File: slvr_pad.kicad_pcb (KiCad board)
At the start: 2 copper layers, 24 parts, among them SW1 SW_Push, U1 ATmega32U4-AU, Y1 16MHz

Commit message: PCB: Route all traces
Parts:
- moved C6 9.53 mm to (156.4, 93.7), turned to 90 degrees
- moved C7 9.53 mm to (146.8, 93.7), turned to 270 degrees
- moved C4 4.83 mm to (142.9, 96.0)
- moved USB1 3.18 mm to (146.8, 81.0)
- moved R4 2.86 mm to (138.1, 100.0), turned to 90 degrees
- moved R2 1.60 mm to (141.3, 90.5)
- moved C1 1.59 mm to (138.1, 104.0)
- moved R3 1.59 mm to (138.1, 90.5)
- turned D3 to 90 degrees
- turned D4 to 90 degrees
- turned Y1 to 180 degrees
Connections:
- D2 pad 1: ROW1 -> ROW0
- D3 pad 1: ROW0 -> ROW1
- MX2 pad 1: COL0 -> COL1
- MX3 pad 1: COL1 -> COL0
- U1 pad 27: Net-(U1-Pad27) -> ROW0
- U1 pad 28: Net-(U1-Pad28) -> COL0
- U1 pad 29: Net-(U1-Pad29) -> ROW1
- U1 pad 30: Net-(U1-Pad30) -> COL1
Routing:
- net GND: track 0.00 -> 121.2 mm, vias 0 -> 2
- net +5V: track 0.00 -> 119.9 mm, vias 0 -> 7
- net COL1: track 0.00 -> 52.1 mm, vias 0 -> 1
- net ROW0: track 0.00 -> 50.1 mm, vias 0 -> 3
- net ROW1: track 0.00 -> 46.9 mm, vias 0 -> 3
- net COL0: track 0.00 -> 30.2 mm, vias 0 -> 1
- net Net-(R4-Pad2): track 0.00 -> 23.3 mm, vias 0 -> 2
- net Net-(R2-Pad1): track 0.00 -> 22.2 mm
- net Net-(R3-Pad1): track 0.00 -> 22.0 mm
- net VCC: track 0.00 -> 13.1 mm
- net Net-(C6-Pad1): track 0.00 -> 12.0 mm
- net Net-(C7-Pad1): track 0.00 -> 11.8 mm
- net D-: track 0.00 -> 10.5 mm
- net D+: track 0.00 -> 7.99 mm
- net Net-(D4-Pad2): track 0.00 -> 6.62 mm
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
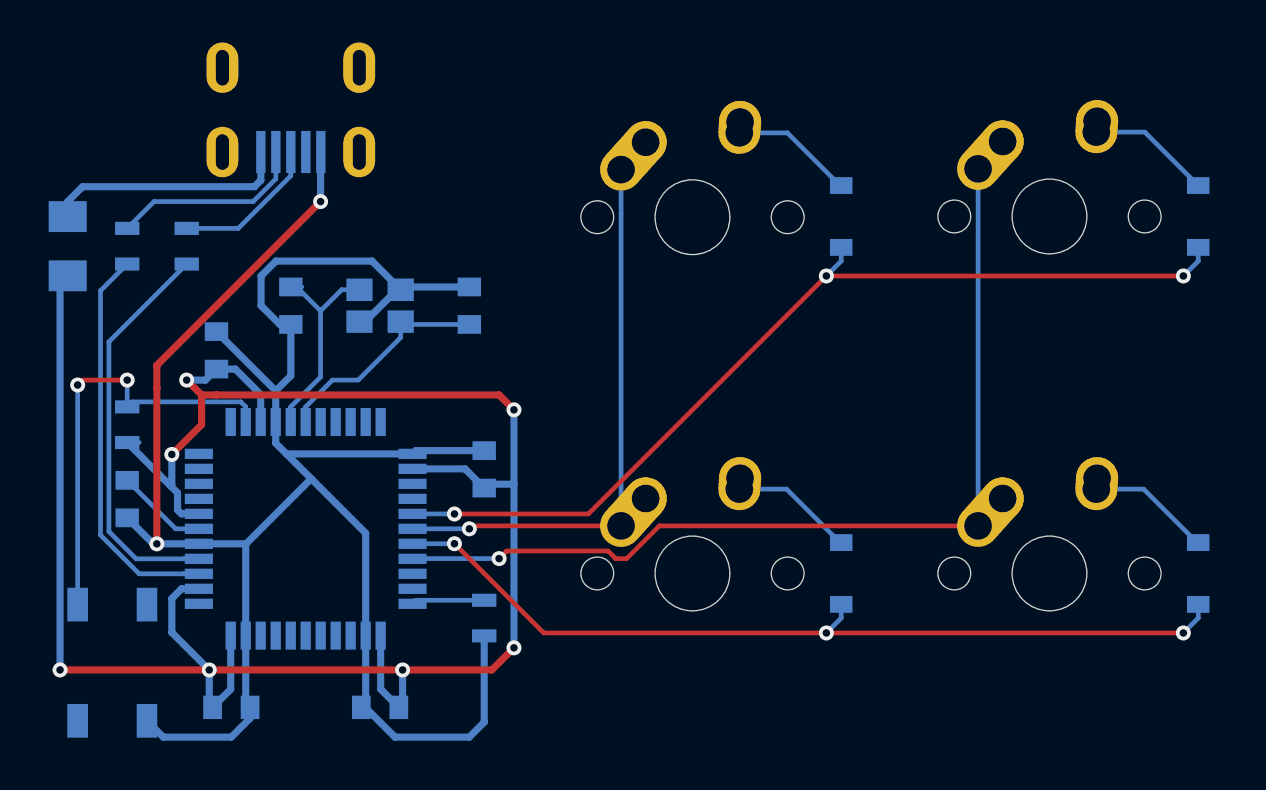
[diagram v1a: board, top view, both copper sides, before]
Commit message: PCB: Add ground fill
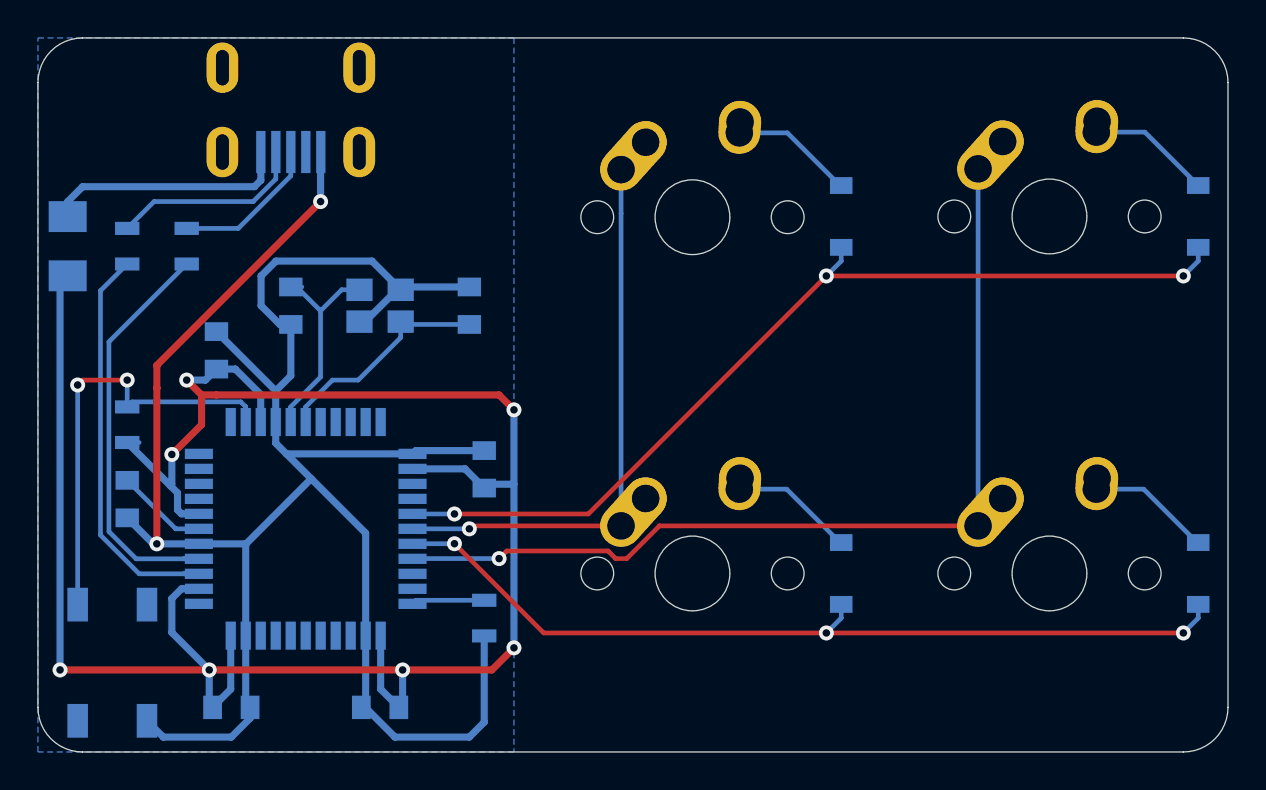
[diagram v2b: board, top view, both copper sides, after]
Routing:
- added copper zone on B.Cu, net GND
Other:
- board outline added: 63.5 x 38.1 mm
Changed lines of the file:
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@@
     (pad_to_mask_clearance 0.05)
     (aux_axis_origin 0 0)
-    (visible_elements FFFFFF7F)
+    (visible_elements FFFDFF7F)
     (pcbplotparams
       (layerselection 0x010fc_ffffffff)
@@
   )
   (module MX_Alps_Hybrid:MX-1U-NoLED (layer F.Cu)
+    (at 187.325 88.9)
+    (fp_text reference MX2 (at 0 3.175) (layer Dwgs.User)
+      (effects (font (size 1 1) (thickness 0.15)))
+    )
+    (fp_text value MX-NoLED (at 0 -7.9375) (layer Dwgs.User)
+      (effects (font (size 1 1) (thickness 0.15)))
+    )
+    (fp_line (start 5 -7) (end 7 -7) (layer Dwgs.User) (width 0.15))
+    (fp_line (start 7 -7) (end 7 -5) (layer Dwgs.User) (width 0.15))
+    (fp_line (start 5 7) (end 7 7) (layer Dwgs.User) (width 0.15))
+    (fp_line (start 7 7) (end 7 5) (layer Dwgs.User) (width 0.15))
+    (fp_line (start -7 5) (end -7 7) (layer Dwgs.User) (width 0.15))
+    (fp_line (start -7 7) (end -5 7) (layer Dwgs.User) (width 0.15))
+    (fp_line (start -5 -7) (end -7 -7) (layer Dwgs.User) (width 0.15))
+    (fp_line (start -7 -7) (end -7 -5) (layer Dwgs.User) (width 0.15))
+    (fp_line (start -9.525 -9.525) (end 9.525 -9.525) (layer Dwgs.User) (width 0.15))
+    (fp_line (start 9.525 -9.525) (end 9.525 9.525) (layer Dwgs.User) (width 0.15))
+    (fp_line (start 9.525 9.525) (end -9.525 9.525) (layer Dwgs.User) (width 0.15))
+    (fp_line (start -9.525 9.525) (end -9.525 -9.525) (layer Dwgs.User) (width 0.15))
+    (pad "" np_thru_hole circle (at 5.08 0 48.0996) (size 1.75 1.75) (drill 1.75) (layers *.Cu *.Mask))
+    (pad "" np_thru_hole circle (at -5.08 0 48.0996) (size 1.75 1.75) (drill 1.75) (layers *.Cu *.Mask))
+    (pad 1 thru_hole circle (at -2.5 -4) (size 2.25 2.25) (drill 1.47) (layers *.Cu B.Mask)
+      (net 14 COL1))
+    (pad "" np_thru_hole circle (at 0 0) (size 3.9878 3.9878) (drill 3.9878) (layers *.Cu *.Mask))
+    (pad 1 thru_hole oval (at -3.81 -2.54 48.0996) (size 4.211556 2.25) (drill 1.47 (offset 0.980778 0)) (layers *.Cu B.Mask)
+      (net 14 COL1))
+    (pad 2 thru_hole circle (at 2.54 -5.08) (size 2.25 2.25) (drill 1.47) (layers *.Cu B.Mask)
+      (net 9 "Net-(D2-Pad2)"))
+    (pad 2 thru_hole oval (at 2.5 -4.5 86.0548) (size 2.831378 2.25) (drill 1.47 (offset 0.290689 0)) (layers *.Cu B.Mask)
+      (net 9 "Net-(D2-Pad2)"))
+  )
+  (module MX_Alps_Hybrid:MX-1U-NoLED (layer F.Cu)
     (at 187.325 107.95)
     (fp_text reference MX4 (at 0 3.175) (layer Dwgs.User)
@@
   )
   (module MX_Alps_Hybrid:MX-1U-NoLED (layer F.Cu)
-    (at 187.325 88.9)
-    (fp_text reference MX2 (at 0 3.175) (layer Dwgs.User)
-      (effects (font (size 1 1) (thickness 0.15)))
-    )
-    (fp_text value MX-NoLED (at 0 -7.9375) (layer Dwgs.User)
-      (effects (font (size 1 1) (thickness 0.15)))
-    )
-    (fp_line (start 5 -7) (end 7 -7) (layer Dwgs.User) (width 0.15))
-    (fp_line (start 7 -7) (end 7 -5) (layer Dwgs.User) (width 0.15))
-    (fp_line (start 5 7) (end 7 7) (layer Dwgs.User) (width 0.15))
-    (fp_line (start 7 7) (end 7 5) (layer Dwgs.User) (width 0.15))
-    (fp_line (start -7 5) (end -7 7) (layer Dwgs.User) (width 0.15))
-    (fp_line (start -7 7) (end -5 7) (layer Dwgs.User) (width 0.15))
-    (fp_line (start -5 -7) (end -7 -7) (layer Dwgs.User) (width 0.15))
-    (fp_line (start -7 -7) (end -7 -5) (layer Dwgs.User) (width 0.15))
-    (fp_line (start -9.525 -9.525) (end 9.525 -9.525) (layer Dwgs.User) (width 0.15))
-    (fp_line (start 9.525 -9.525) (end 9.525 9.525) (layer Dwgs.User) (width 0.15))
-    (fp_line (start 9.525 9.525) (end -9.525 9.525) (layer Dwgs.User) (width 0.15))
-    (fp_line (start -9.525 9.525) (end -9.525 -9.525) (layer Dwgs.User) (width 0.15))
-    (pad "" np_thru_hole circle (at 5.08 0 48.0996) (size 1.75 1.75) (drill 1.75) (layers *.Cu *.Mask))
-    (pad "" np_thru_hole circle (at -5.08 0 48.0996) (size 1.75 1.75) (drill 1.75) (layers *.Cu *.Mask))
-    (pad 1 thru_hole circle (at -2.5 -4) (size 2.25 2.25) (drill 1.47) (layers *.Cu B.Mask)
-      (net 14 COL1))
-    (pad "" np_thru_hole circle (at 0 0) (size 3.9878 3.9878) (drill 3.9878) (layers *.Cu *.Mask))
-    (pad 1 thru_hole oval (at -3.81 -2.54 48.0996) (size 4.211556 2.25) (drill 1.47 (offset 0.980778 0)) (layers *.Cu B.Mask)
-      (net 14 COL1))
-    (pad 2 thru_hole circle (at 2.54 -5.08) (size 2.25 2.25) (drill 1.47) (layers *.Cu B.Mask)
-      (net 9 "Net-(D2-Pad2)"))
-    (pad 2 thru_hole oval (at 2.5 -4.5 86.0548) (size 2.831378 2.25) (drill 1.47 (offset 0.290689 0)) (layers *.Cu B.Mask)
-      (net 9 "Net-(D2-Pad2)"))
-  )
-  (module MX_Alps_Hybrid:MX-1U-NoLED (layer F.Cu)
     (at 168.275 88.94)
     (fp_text reference MX1 (at 0 3.175) (layer Dwgs.User)
@@
     )
   )
-  (gr_line (start 132.55625 115.09375) (end 132.55625 81.75625) (layer Dwgs.User) (width 0.15))
-  (gr_line (start 194.46875 117.475) (end 134.9375 117.475) (layer Dwgs.User) (width 0.15))
-  (gr_line (start 196.85 81.75625) (end 196.85 115.09375) (layer Dwgs.User) (width 0.15))
-  (gr_line (start 134.9375 79.375) (end 195.2625 79.375) (layer Dwgs.User) (width 0.15))
-  (gr_arc (start 134.9375 81.75625) (end 134.9375 79.375) (angle -90) (layer Dwgs.User) (width 0.15))
-  (gr_arc (start 134.9375 115.09375) (end 132.55625 115.09375) (angle -90) (layer Dwgs.User) (width 0.15))
-  (gr_arc (start 194.46875 115.09375) (end 194.46875 117.475) (angle -90) (layer Dwgs.User) (width 0.15))
-  (gr_arc (start 194.46875 81.75625) (end 196.85 81.75625) (angle -90) (layer Dwgs.User) (width 0.15))
+  (gr_line (start 194.46875 117.475) (end 135.73125 117.475) (layer Edge.Cuts) (width 0.05))
+  (gr_line (start 196.85 81.75625) (end 196.85 115.09375) (layer Edge.Cuts) (width 0.05))
+  (gr_line (start 135.73125 79.375) (end 194.46875 79.375) (layer Edge.Cuts) (width 0.05))
+  (gr_line (start 133.35 115.09375) (end 133.35 81.75625) (layer Edge.Cuts) (width 0.05))
+  (gr_arc (start 135.73125 81.75625) (end 135.73125 79.375) (angle -90) (layer Edge.Cuts) (width 0.05))
+  (gr_arc (start 135.73125 115.09375) (end 133.35 115.09375) (angle -90) (layer Edge.Cuts) (width 0.05))
+  (gr_arc (start 194.46875 115.09375) (end 194.46875 117.475) (angle -90) (layer Edge.Cuts) (width 0.05))
+  (gr_arc (start 194.46875 81.75625) (end 196.85 81.75625) (angle -90) (layer Edge.Cuts) (width 0.05))
   (segment (start 140.7 105.56875) (end 141.9375 105.56875) (width 0.25) (layer B.Cu) (net 1))
   (segment (start 138.1125 102.98125) (end 140.7 105.56875) (width 0.25) (layer B.Cu) (net 1))
@@
   (via (at 138.1125 97.63125) (size 0.8) (drill 0.4) (layers F.Cu B.Cu) (net 20))
   (segment (start 138.1125 97.63125) (end 138.1125 99.0625) (width 0.25) (layer B.Cu) (net 20))
+  (zone (net 2) (net_name GND) (layer B.Cu) (hatch edge 0.508)
+    (connect_pads (clearance 0.508))
+    (min_thickness 0.254)
+    (fill yes (arc_segments 32) (thermal_gap 0.508) (thermal_bridge_width 0.508))
+    (polygon
+      (pts
+        (xy 158.75 117.475) (xy 133.35 117.475) (xy 133.35 79.375) (xy 158.75 79.375)
+      )
+    )
+  )
 )

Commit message: PCB: Add 3D components and fix warnings
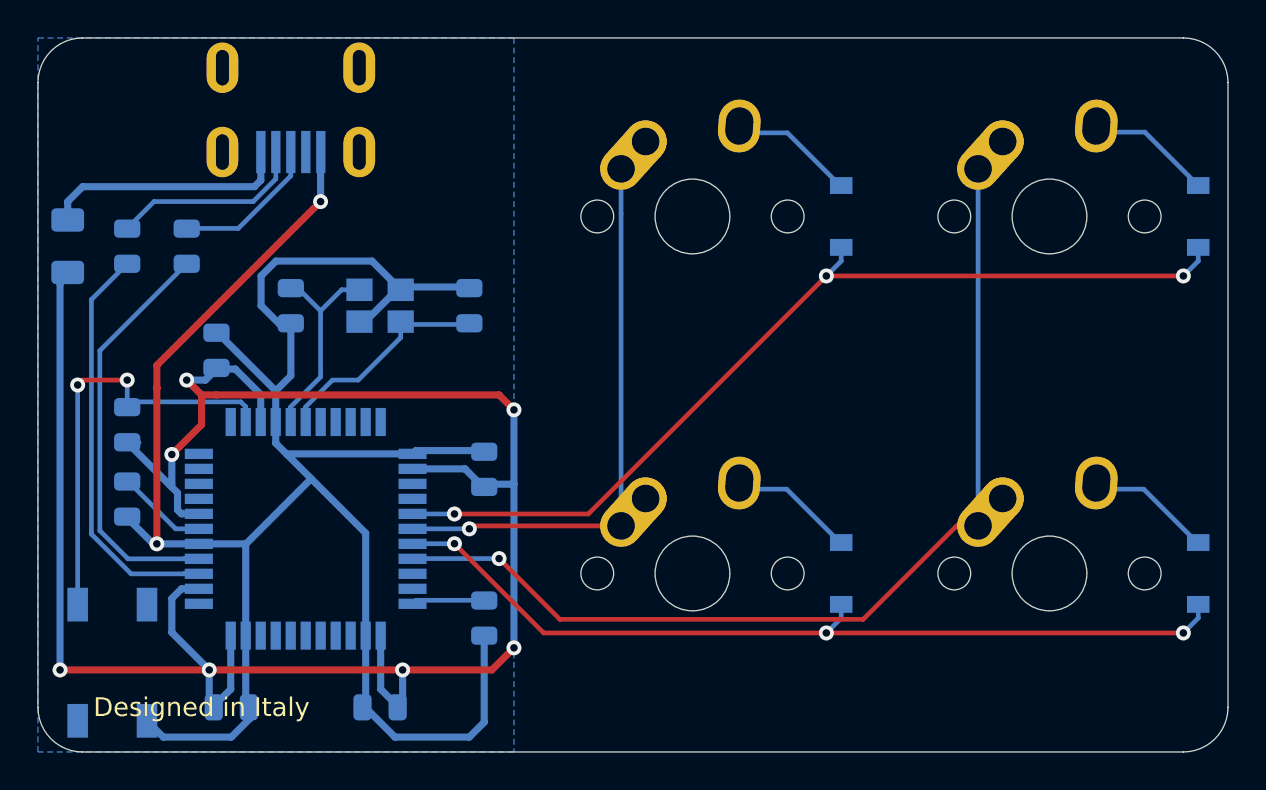
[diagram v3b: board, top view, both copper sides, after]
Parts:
- C1, C2, C3, C4, C5, C6, C7: footprint Capacitors_SMD:C_0805 -> Capacitor_SMD:C_0805_2012Metric
- D1, D2, D3, D4: footprint Diodes_SMD:D_SOD-123 -> Diode_SMD:D_SOD-123
- F1: footprint Fuse_Holders_and_Fuses:Fuse_SMD1206_Wave -> Fuse:Fuse_1206_3216Metric
- R1, R2, R3, R4: footprint Resistors_SMD:R_0805 -> Resistor_SMD:R_0805_2012Metric
- U1: footprint Housings_QFP:TQFP-44_10x10mm_Pitch0.8mm -> Package_QFP:TQFP-44_10x10mm_P0.8mm
- Y1: footprint Crystals:Crystal_SMD_3225-4pin_3.2x2.5mm -> Crystal:Crystal_SMD_3225-4Pin_3.2x2.5mm
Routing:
- net COL1: track 52.1 -> 54.5 mm
- net Net-(R3-Pad1): track 22.0 -> 22.6 mm
- net Net-(R2-Pad1): track 22.2 -> 22.9 mm
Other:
- board text added: "Designed in Italy"
